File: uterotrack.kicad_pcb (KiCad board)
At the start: 4 copper layers, 34 x 98 mm, 139 parts, among them J1 RFShield, J2 MicroSD_Card, J3 Argos_Prog, J4 AS5510, J5 Prog, J6 EXP, Q1 DMP2110UW, Q10 MMBT2222, Q11 MMBT2222, Q12 MMBT2222, Q13 MMBT2222, Q14 SiS454DN, Q15 SiS454DN, Q16 SiS415DNT, Q17 MMBT4403, Q18 MMBT2222, Q2 DMP2110UW, Q3 MMBT2222, Q4 DMP2110UW, Q5 DMP2110UW, Q6 MMBT2222, Q7 SiS415DNT, Q8 DMP2110UW, Q9 MMBT2222, U1 Argos_SMD, U10 AH1806-W, U11 LTC3221EDC-3.3, U2 ESP32-S3-WROOM-1, U3 keller_6LHPD, U4 RV-3032-C7, U5 CAM-M8Q, U6 BQ29732, U7 BQ51050BRHL, U8 TPS63001, U9 TPS63900

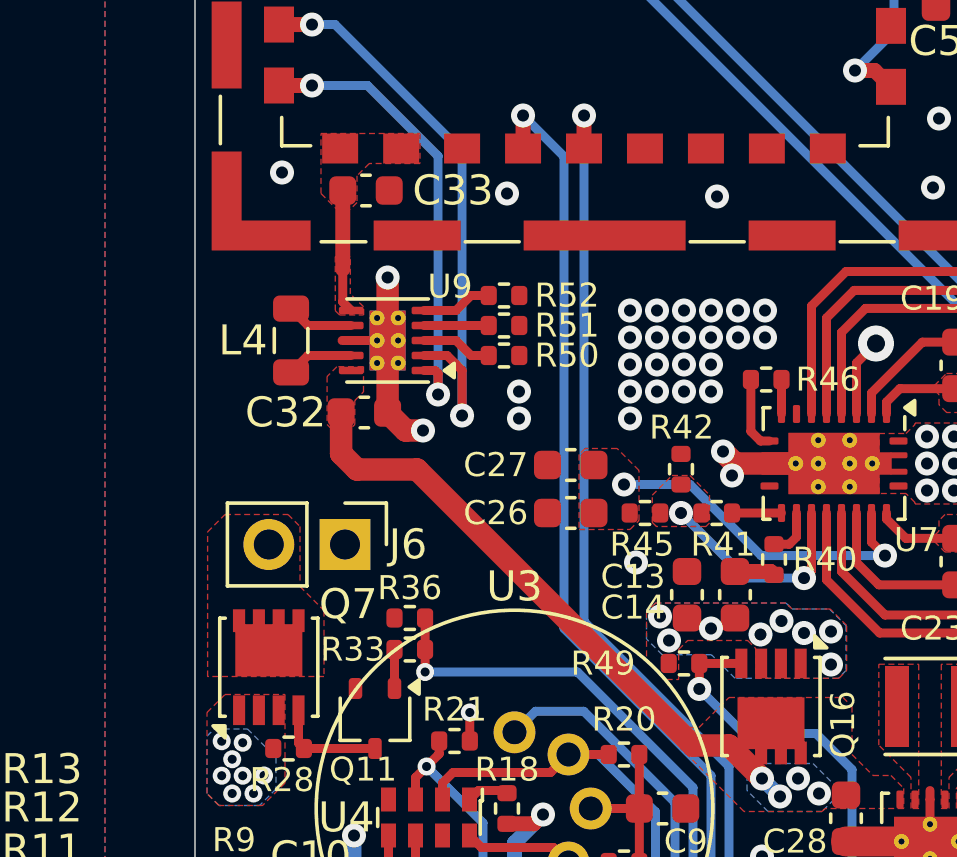
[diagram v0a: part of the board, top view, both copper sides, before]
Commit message: Fix all the errors, except overlap of uSD and battery
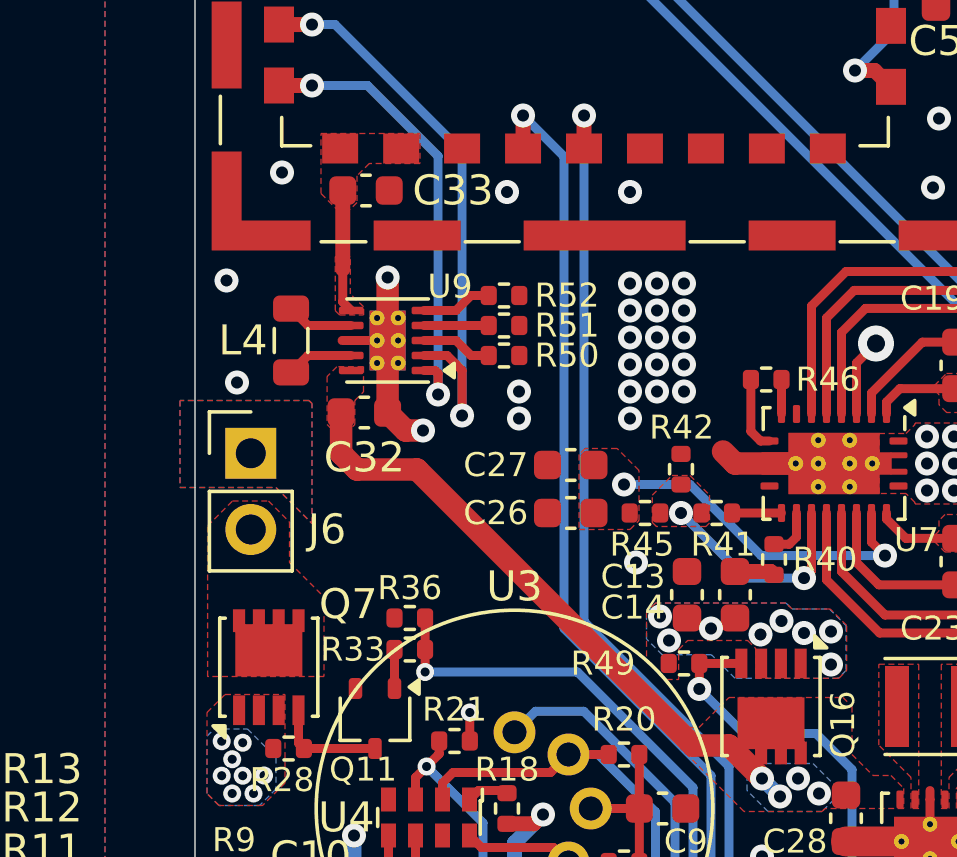
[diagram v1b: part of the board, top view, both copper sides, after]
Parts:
- moved J6 4.37 mm to (134.9, 102.9), turned to 0 degrees
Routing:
- net GND: vias 106 -> 101

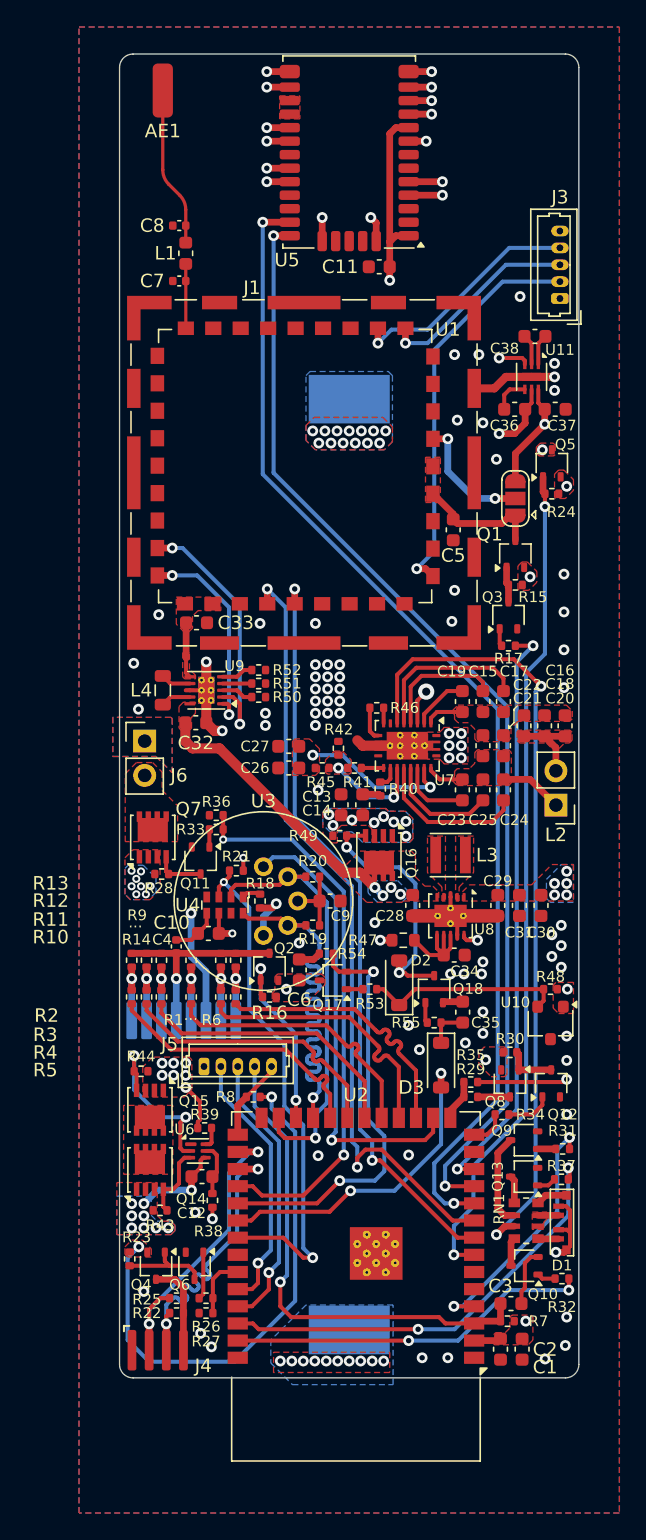
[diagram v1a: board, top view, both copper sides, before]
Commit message: Fix warning as possible in F.SilkS
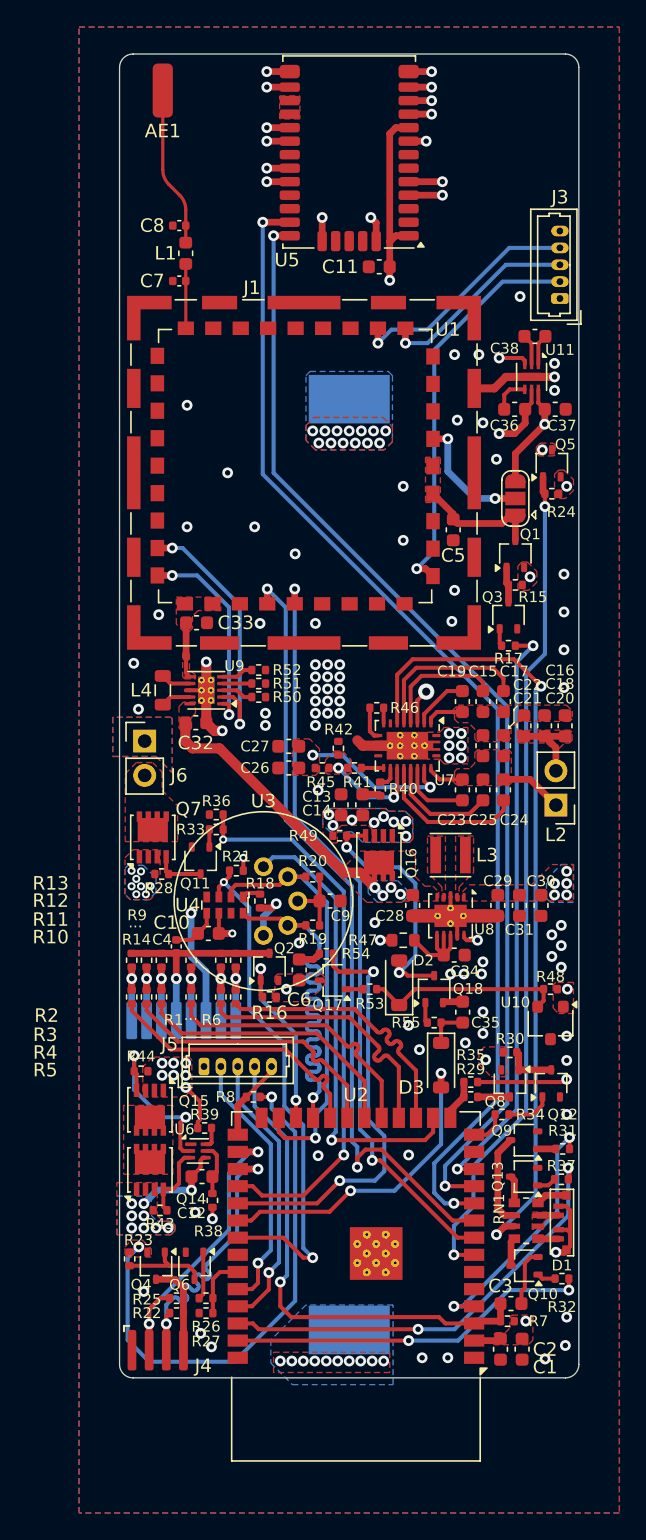
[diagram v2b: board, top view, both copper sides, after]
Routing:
- net GND: vias 101 -> 108
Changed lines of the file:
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@@
 		(tags "capacitor")
 		(property "Reference" "C31"
-			(at 2 0 0)
+			(at 1.8 0 0)
 			(layer "F.SilkS")
 			(effects
@@
 		(tags "SOT-323 SC-70")
 		(property "Reference" "Q1"
-			(at 1.45 -1.91 180)
+			(at 1.45 1.1 180)
 			(layer "F.SilkS")
 			(effects
 				(font
-					(size 1 1)
-					(thickness 0.15)
+					(size 0.8 0.8)
+					(thickness 0.11)
 				)
 			)
@@
 		(tags "resistor")
 		(property "Reference" "R43"
-			(at 0 1.1 0)
+			(at 0 1 0)
 			(layer "F.SilkS")
 			(effects
@@
 	(footprint "Resistor_SMD:R_0402_1005Metric"
 		(layer "F.Cu")
-		(at 140.16 108.35 180)
+		(at 140.16 108.3 180)
 		(descr "Resistor SMD 0402 (1005 Metric), square (rectangular) end terminal, IPC-7351 nominal, (Body size source: IPC-SM-782 page 72, https://www.pcb-3d.com/wordpress/wp-content/uploads/ipc-sm-782a_amendment_1_and_2.pdf), generated with kicad-footprint-generator")
 		(tags "resistor")
@@
 		(tags "resistor")
 		(property "Reference" "R54"
-			(at 1.9 0 0)
+			(at 2.2 0 0)
 			(layer "F.SilkS")
 			(effects
@@
 		(tags "SOD-123")
 		(property "Reference" "D2"
-			(at 1.65 1.6 180)
+			(at 1.65 1.8 180)
 			(layer "F.SilkS")
 			(effects
@@
 		(tags "resistor")
 		(property "Reference" "R23"
-			(at -1.6 -0.51 0)
+			(at -1.39 -0.65 0)
 			(layer "F.SilkS")
 			(effects
@@
 		(tags "capacitor")
 		(property "Reference" "C30"
-			(at 2 0 0)
+			(at -1.8 0 0)
 			(layer "F.SilkS")
 			(effects
@@
 			(net 0)
 			(net_name "")
-			(layers "F.Cu" "B.Cu")
+			(layers "F.Cu" "B.Cu" "In1.Cu" "In2.Cu")
 			(hatch full 0.508)
 			(connect_pads
@@
 			(at 0 8.25 180)
 			(layer "F.Fab")
+			(hide yes)
 			(effects
 				(font
@@
 			(net 0)
 			(net_name "")
-			(layers "F.Cu" "B.Cu")
+			(layers "F.Cu" "B.Cu" "In1.Cu" "In2.Cu")
 			(hatch edge 0.5)
 			(connect_pads
@@
 	)
 	(via
+		(at 143 87)
+		(size 0.8)
+		(drill 0.4)
+		(layers "F.Cu" "B.Cu")
+		(free yes)
+		(net 5)
+	)
+	(via
 		(at 134.05 97.1)
 		(size 0.8)
@@
 	)
 	(via
+		(at 154 84)
+		(size 0.8)
+		(drill 0.4)
+		(layers "F.Cu" "B.Cu")
+		(free yes)
+		(net 5)
+	)
+	(via
 		(at 143.8 101.7)
 		(size 0.8)
@@
 	)
 	(via
+		(at 138 78)
+		(size 0.8)
+		(drill 0.4)
+		(layers "F.Cu" "B.Cu")
+		(free yes)
+		(net 5)
+	)
+	(via
 		(at 166.1 145.5)
 		(size 0.8)
@@
 	)
 	(via
+		(at 154 88)
+		(size 0.8)
+		(drill 0.4)
+		(layers "F.Cu" "B.Cu")
+		(free yes)
+		(net 5)
+	)
+	(via
 		(at 159.9 124.5)
 		(size 0.8)
@@
 	)
 	(via
+		(at 138 87)
+		(size 0.8)
+		(drill 0.4)
+		(layers "F.Cu" "B.Cu")
+		(free yes)
+		(net 5)
+	)
+	(via
 		(at 164.5 148.6)
 		(size 0.8)
@@
 	)
 	(via
+		(at 146 89)
+		(size 0.8)
+		(drill 0.4)
+		(layers "F.Cu" "B.Cu")
+		(free yes)
+		(net 5)
+	)
+	(via
 		(at 156.1 54.45)
 		(size 0.8)
@@
 	)
 	(via
+		(at 141 83)
+		(size 0.8)
+		(drill 0.4)
+		(layers "F.Cu" "B.Cu")
+		(free yes)
+		(net 5)
+	)
+	(via
 		(at 154.4 123.9)
 		(size 0.8)
@@
 	)
 	(segment
-		(start 140.67 108.35)
-		(end 140.67 110.15)
+		(start 149.6 133.5)
+		(end 146.6 136.5)
 		(width 0.3)
 		(layer "F.Cu")
@@
 	)
 	(segment
-		(start 149.6 133.5)
-		(end 146.6 136.5)
+		(start 140.67 108.3)
+		(end 140.67 110.15)
 		(width 0.3)
 		(layer "F.Cu")

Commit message: Move battery 1.5mm down
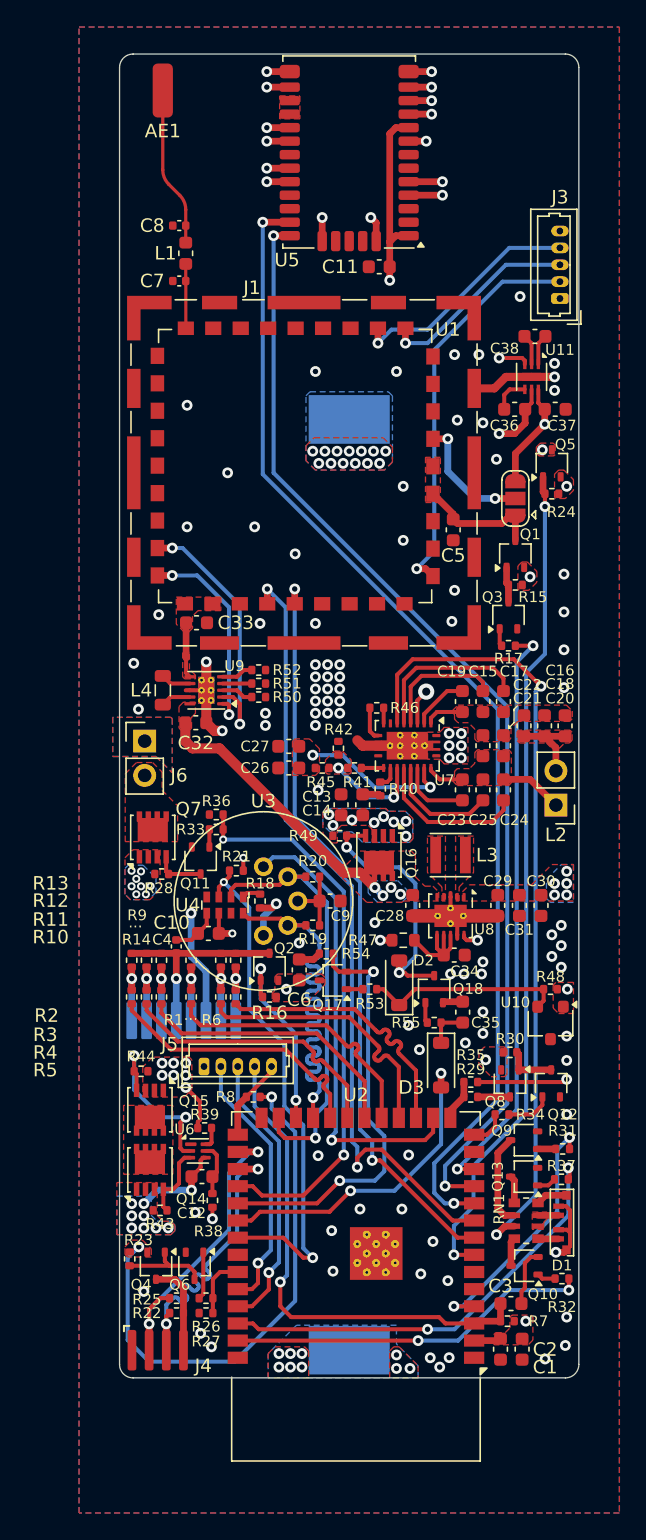
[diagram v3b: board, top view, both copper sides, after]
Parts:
- moved BT1 1.50 mm to (150.0, 113.5)
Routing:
- net /Batt: track 177.9 -> 174.5 mm
- net GND: vias 108 -> 118
- net /power/BAT-: vias 19 -> 18

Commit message: Remake PCB led RGB circuit
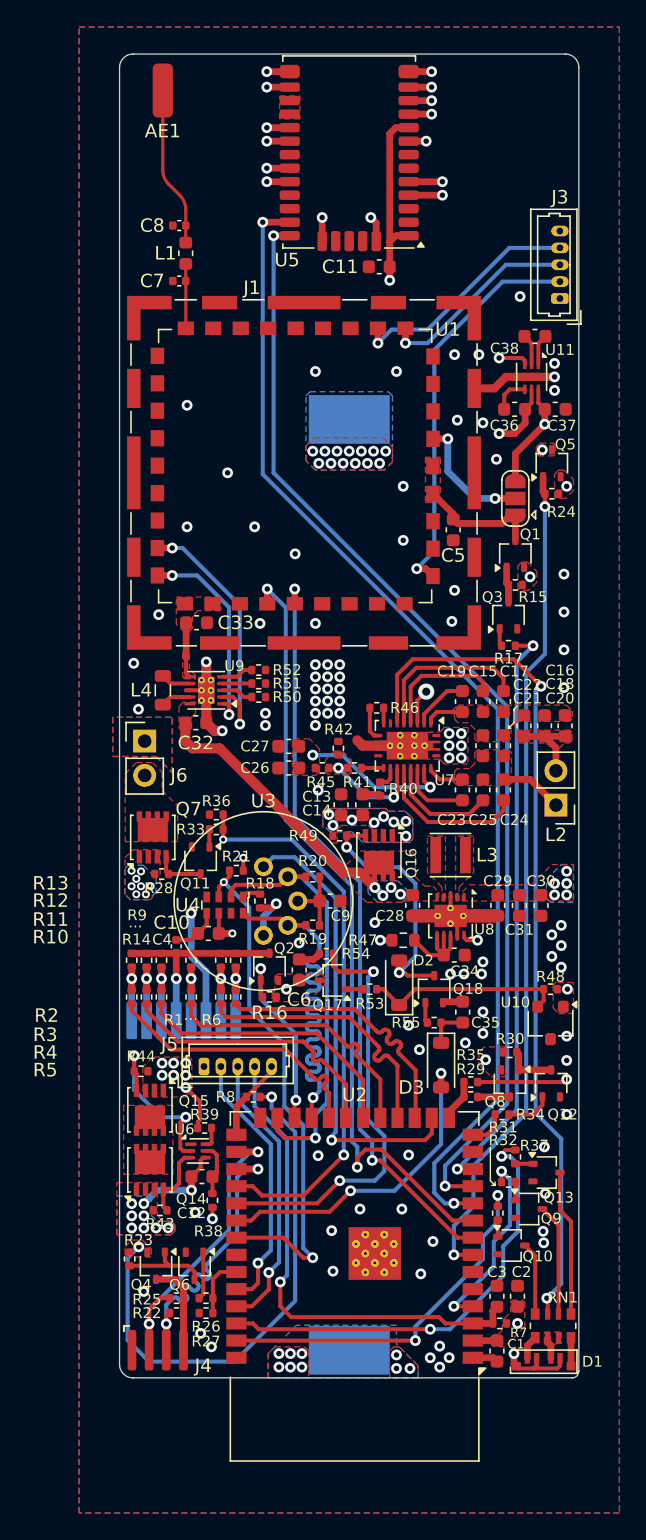
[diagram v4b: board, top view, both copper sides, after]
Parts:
- moved D1 10.4 mm to (164.4, 148.8), turned to 0 degrees
- moved RN1 8.03 mm to (165.1, 146.2), turned to -90 degrees
- moved R32 6.79 mm to (161.0, 137.8), turned to -90 degrees
- moved Q9 5.11 mm to (163.3, 137.5), turned to 0 degrees
- moved R31 4.70 mm to (161.8, 135.5), turned to 0 degrees
- moved C2 3.93 mm to (162.5, 144.0), turned to -90 degrees
- moved R37 3.79 mm to (162.3, 133.6), turned to -90 degrees
- moved Q10 1.79 mm to (162.0, 140.2), turned to 0 degrees
- moved Q13 1.68 mm to (164.6, 134.8), turned to 0 degrees
- moved C3 1.17 mm to (160.9, 144.0), turned to 90 degrees
- moved R7 0.59 mm to (161.1, 146.0)
- moved C1 0.30 mm to (160.9, 148.0)
- moved U2 0.10 mm to (150.4, 143.2)
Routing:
- net Net-(Q13-C): track 2.06 -> 10.8 mm
- net /Red: track 18.8 -> 14.2 mm
- net /Charge: track 59.1 -> 63.5 mm
- net Net-(Q10-C): track 2.11 -> 5.39 mm
- net GND: track 92.1 -> 89.7 mm, vias 118 -> 119
- net /Batt: track 174.5 -> 176.3 mm
- net Net-(Q9-C): track 6.90 -> 8.27 mm
- net /Green: track 32.5 -> 33.1 mm
- net /RST: track 37.1 -> 36.6 mm
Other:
- outline, holes or cut-outs redrawn
